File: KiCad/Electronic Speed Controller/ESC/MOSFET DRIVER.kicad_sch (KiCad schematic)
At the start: 0 parts

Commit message: Create MOSFETs driver schematic
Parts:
- added C18: 6p8, symbol Device:C
- added C19: 120p, symbol Device:C
- added C20: 2u2, symbol Device:C
- added C21: 0u022, symbol Device:C
- added C22, C25: 1u, symbol Device:C
- added C23, C24: 2200p, symbol Device:C
- added C26: 0u015, symbol Device:C
- added C27, C29, C31, C32, C33, C34: 0u1, symbol Device:C
- added C28, C35: 4u7, symbol Device:C
- added C30: 47u, symbol Device:C
- added D4: D, symbol Device:D
- added L1: 22u, symbol Device:L
- added R11: 205k, symbol Device:R
- added R12: 16k2, symbol Device:R
- added R13, R15, R16, R17: 10k, symbol Device:R
- added R14: 31k6, symbol Device:R
- added R18: 1k, symbol Device:R
- added R19, R20: 56, symbol Device:R
- added R21: 1M, symbol Device:R
- added U2: DRV8302DCA, DCA56_6P35X3P61, symbol DRV8302:DRV8302DCA
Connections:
- new net: C31.1, U2.48 (BST_A)
- new net: C31.2, U2.46 (SH_A)
- new net: C25.2, U2.27 (AVDD)
- new net: C20.2, U2.13 (GVDD)
- new net: C33.1, U2.38 (BST_C)
- new net: C33.2, U2.36 (SH_C)
- new net: R11.2, U2.1 (RT_CLK)
- new net: C21.2, U2.14 (CP1)
- new net: C21.1, U2.15 (CP2)
- new net: C19.1, R12.1, U2.2 (COMP)
- new net: C22.2, U2.23 (DVDD)
- new net: R19.2, U2.25 (SO1)
- new net: R20.2, U2.26 (SO2)
- new net: R13.1, R14.2, U2.3 (VSENSE)
- new net: R15.2, U2.4 (PWRGD)
- new net: C32.2, U2.41 (SH_B)
- new net: C32.1, U2.43 (BST_B)
- new net: R21.1, U2.49 (BIAS)
- new net: R16.2, U2.5 (*OCTW)
- new net: C29.2, D4.1 (K), L1.1, U2.50 (PH), U2.51 (PH)
- new net: C29.1, U2.52 (BST_BK)
- new net: C26.2, U2.56 (SS_TR)
- new net: R17.2, U2.6 (*FAULT)
- new net: R18.2, U2.7 (DTC)
- new net: C18.1, R12.2
- new net: C23.1, C24.1, R20.1
- new net GND: C18.2, C19.2, C20.1, C22.1, C23.2, C24.2, C25.1, C26.1, C27.2, C28.2, C30.2, C34.2, C35.2, D4.2 (A), R11.1, R13.2, R18.1, R21.2, U2.28 (AGND), U2.57 (EPAD)
- new net PVDD: C27.1, C28.1, C34.1, C35.1, U2.29 (PVDD1), U2.53 (PVDD2), U2.54 (PVDD2)
- new net VCC: C30.1, L1.2, R14.1, R15.1, R16.1, R17.1
- no-connect marks 0 -> 1
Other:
- note added: "${TITLE}"
- title: (none) -> MOSFET Driver

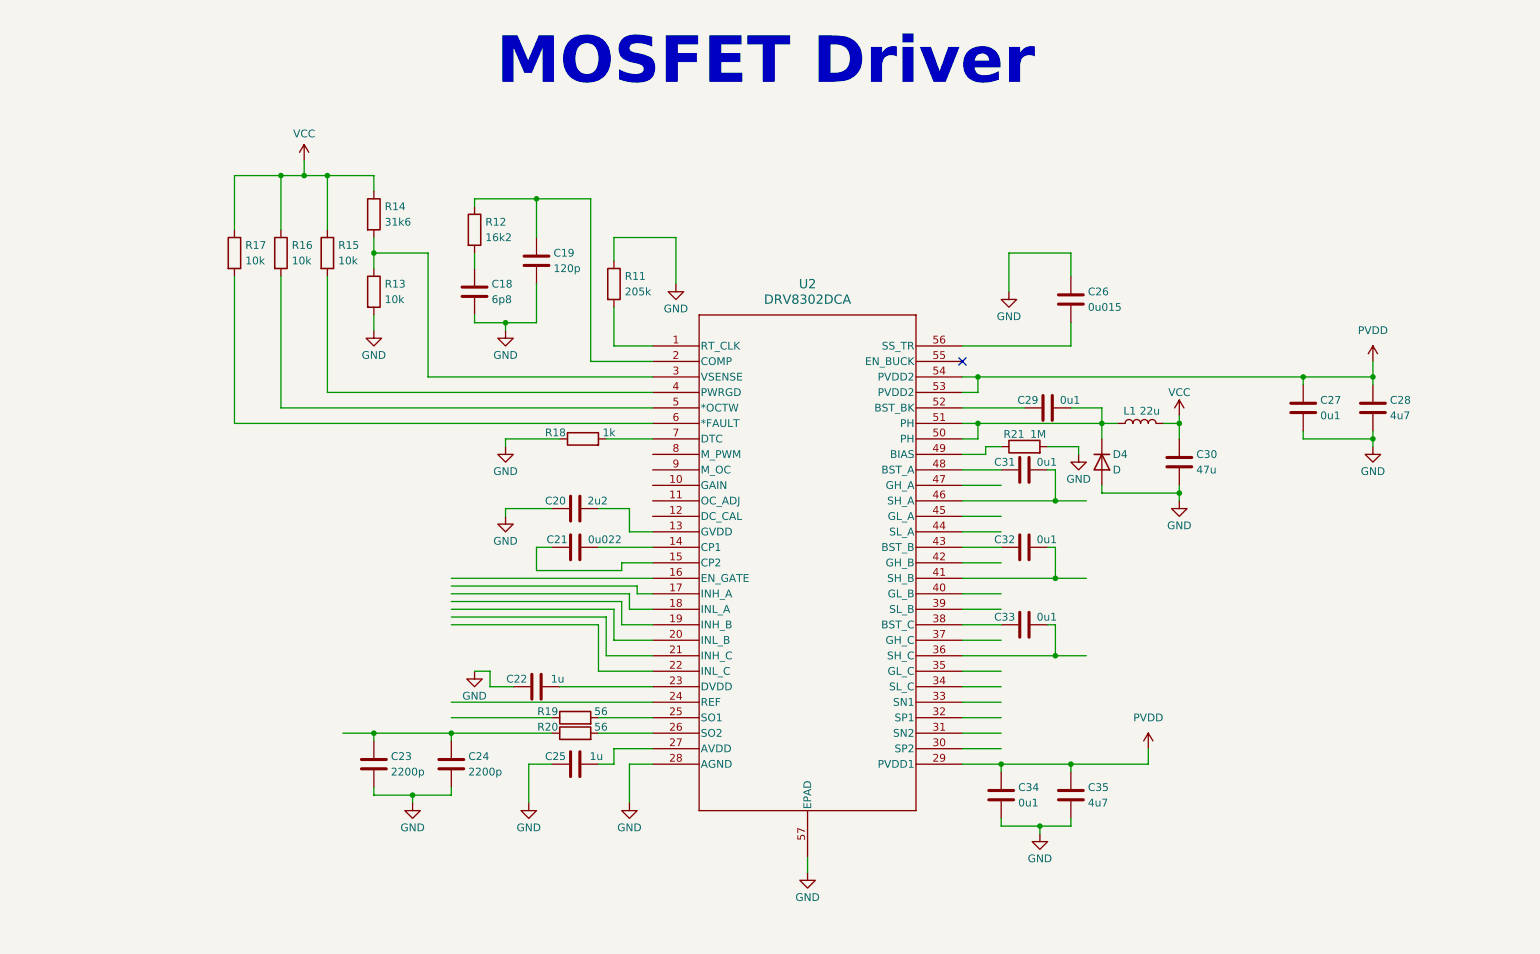
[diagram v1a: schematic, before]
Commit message: Update MOSFETs driver schematic
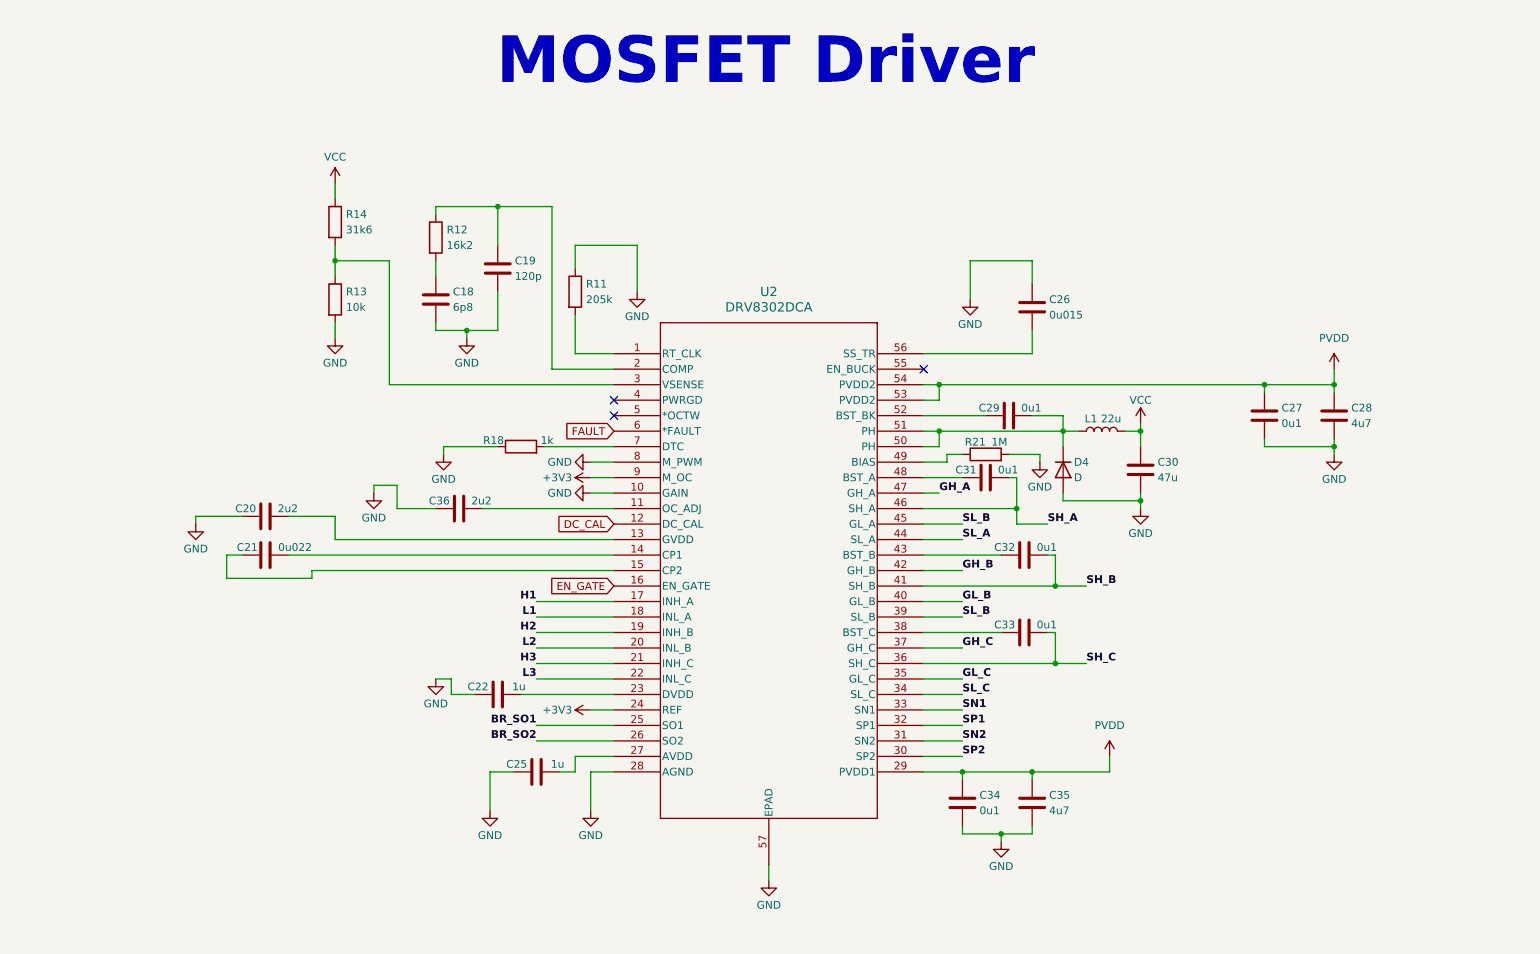
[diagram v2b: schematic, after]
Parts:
- removed C23, C24: 2200p, symbol Device:C
- removed R15, R16, R17: 10k, symbol Device:R
- removed R19, R20: 56, symbol Device:R
- added C36: 2u2, symbol Device:C
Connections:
- net GND: now also U2.10 (GAIN), U2.8 (M_PWM), C36.1
- net SH_A: now reaches C31.2, U2.46 (SH_A)
- net SH_C: now reaches C33.2, U2.36 (SH_C)
- net at U2.11 (OC_ADJ): now also C36.2
- net DC_CAL: now reaches U2.12 (DC_CAL)
- net EN_GATE: now reaches U2.16 (EN_GATE)
- net H1: now reaches U2.17 (INH_A)
- net L1: now reaches U2.18 (INL_A)
- net H2: now reaches U2.19 (INH_B)
- net L2: now reaches U2.20 (INL_B)
- net H3: now reaches U2.21 (INH_C)
- net L3: now reaches U2.22 (INL_C)
- net +3V3: now reaches U2.24 (REF)
- net +3V3: now also U2.9 (M_OC)
- net BR_SO1: now reaches U2.25 (SO1)
- net BR_SO2: now reaches U2.26 (SO2)
- net SP2: now reaches U2.30 (SP2)
- net SN2: now reaches U2.31 (SN2)
- net SP1: now reaches U2.32 (SP1)
- net SN1: now reaches U2.33 (SN1)
- net SL_C: now reaches U2.34 (SL_C)
- net GL_C: now reaches U2.35 (GL_C)
- net GH_C: now reaches U2.37 (GH_C)
- net SL_B: now reaches U2.39 (SL_B)
- net SL_B: now also U2.45 (GL_A)
- net GL_B: now reaches U2.40 (GL_B)
- net SH_B: now reaches C32.2, U2.41 (SH_B)
- net GH_B: now reaches U2.42 (GH_B)
- net SL_A: now reaches U2.44 (SL_A)
- net GH_A: now reaches U2.47 (GH_A)
- net FAULT: now reaches U2.6 (*FAULT)
- no-connect marks 1 -> 3
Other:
- moved on the sheet: C18, C19, C20, C21, C22, C25, C26, C27, C28, C29, C30, C31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

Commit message: Add MOSFETs driver input ports
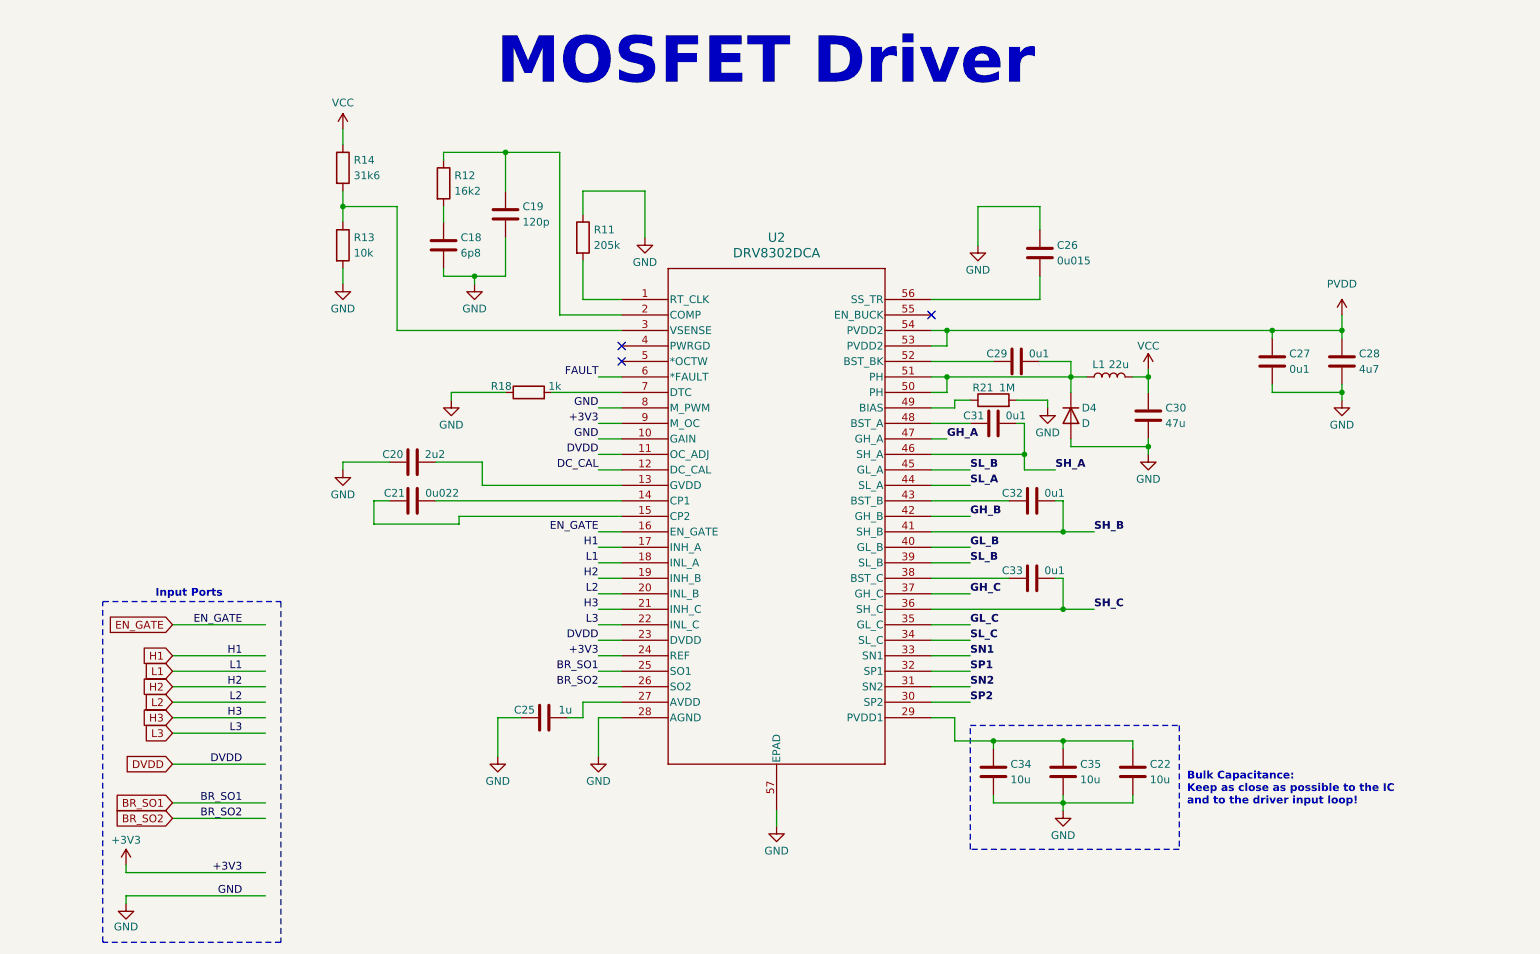
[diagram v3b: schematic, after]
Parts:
- removed C36: 2u2, symbol Device:C
- C22: value 1u -> 10u
- C34: value 0u1 -> 10u
- C35: value 4u7 -> 10u
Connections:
- net GND: now also C22.2; no longer C22.1
- net PVDD: no longer C34.1, C35.1, U2.29 (PVDD1)
- net DVDD: now reaches U2.11 (OC_ADJ)
- net DVDD: now also U2.23 (DVDD)
- new net: C22.1, C34.1, C35.1, U2.29 (PVDD1)
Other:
- note added: "Bulk Capacitance: Keep as close as possible to the IC and to the driver input loop!"
- note added: "Input Ports"
- moved on the sheet: C18, C19, C20, C21, C25, C26, C27, C28, C29, C30, C31, C32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

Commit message: Update MOSFETs driver schematic
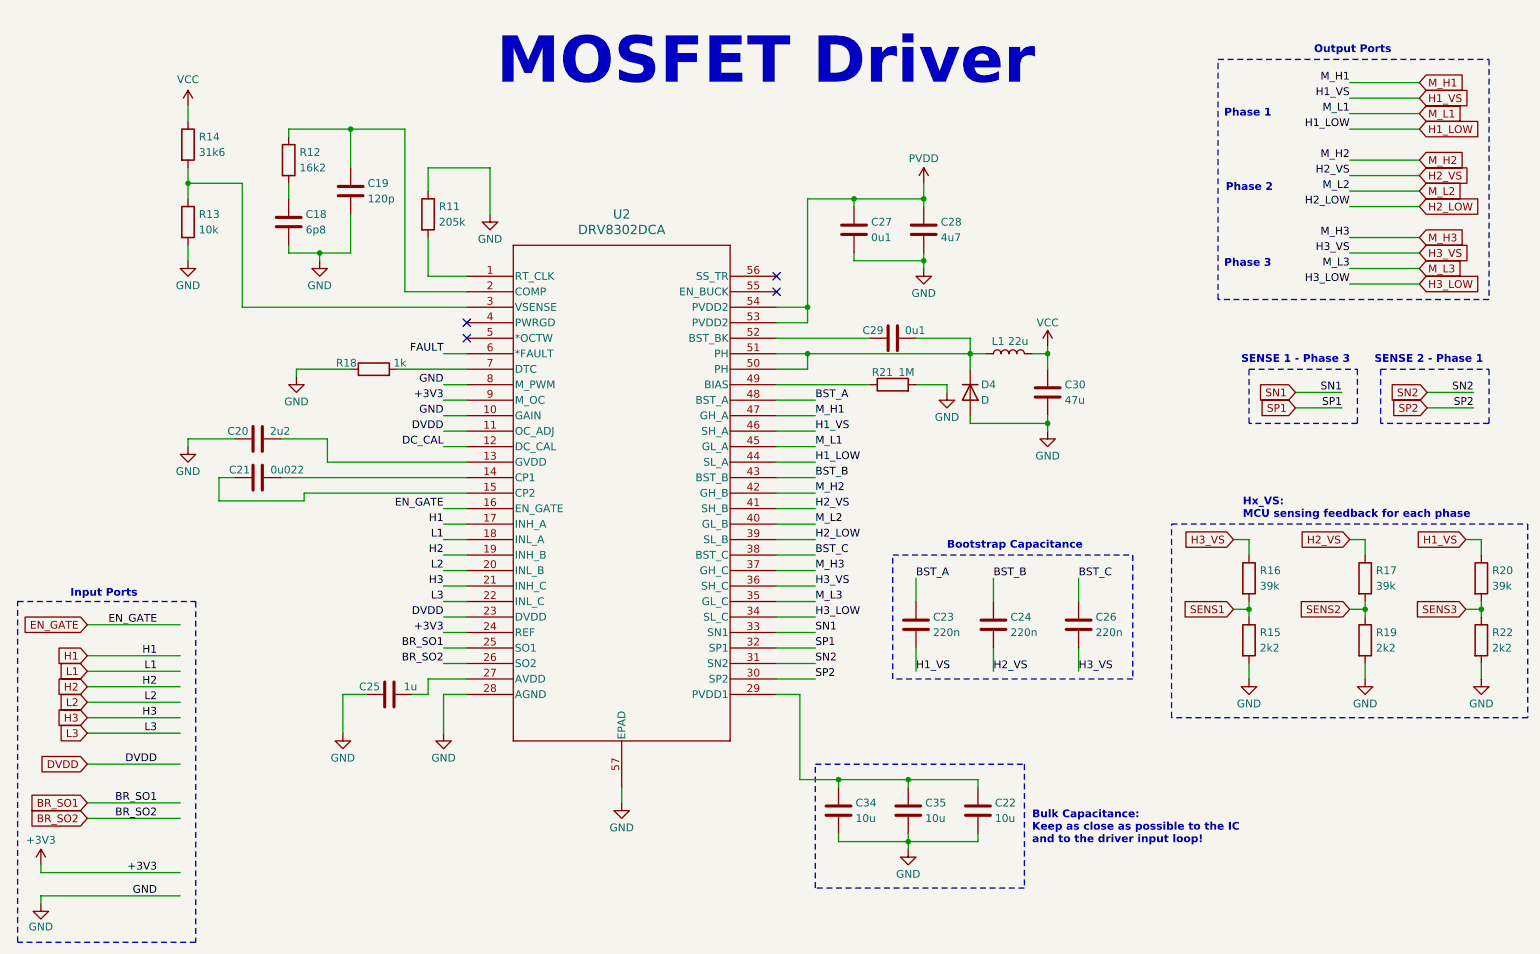
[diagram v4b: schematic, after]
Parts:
- removed C31, C32, C33: 0u1, symbol Device:C
- added C23, C24: 220n, symbol Device:C
- added R15, R19, R22: 2k2, symbol Device:R
- added R16, R17, R20: 39k, symbol Device:R
- C26: value 0u015 -> 220n
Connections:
- net GND: now also R15.2, R19.2, R22.2; no longer C26.1
- net BST_A: now reaches U2.48 (BST_A)
- net BST_A: now also C23.1
- net BST_C: now reaches U2.38 (BST_C)
- net BST_C: now also C26.1
- net BST_B: now reaches U2.43 (BST_B)
- net BST_B: now also C24.1
- net at U2.56 (SS_TR): no longer C26.2
- net GH_A renamed M_H1
- net GH_B renamed M_H2
- net GH_C renamed M_H3
- net GL_B renamed M_L2
- net GL_C renamed M_L3
- net SH_A renamed H1_VS
- net H1_VS: now also C23.2, R20.1
- net SH_B renamed H2_VS
- net H2_VS: now also C24.2, R17.1
- net SH_C renamed H3_VS
- net H3_VS: now also C26.2, R16.1
- net SL_A renamed H1_LOW
- net SL_B renamed H2_LOW
- net H2_LOW: no longer U2.45 (GL_A)
- net SL_C renamed H3_LOW
- new net M_L1: U2.45 (GL_A)
- new net SENS1: R15.1, R16.2
- new net SENS2: R17.2, R19.1
- new net SENS3: R20.2, R22.1
- no-connect marks 3 -> 4
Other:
- note added: "Bootstrap Capacitance"
- note added: "Hx_VS: MCU sensing feedback for each phase"
- note added: "Output Ports"
- note added: "Phase 1"
- note added: "Phase 2"
- note added: "Phase 3"
- note added: "SENSE 1 - Phase 3"
- note added: "SENSE 2 - Phase 1"
- moved on the sheet: C18, C19, C20, C21, C22, C25, C27, C28, C29, C30, C34, C35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
